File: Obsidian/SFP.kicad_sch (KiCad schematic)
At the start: 42 parts, among them J1 TYCO_1888247-1, J12 TYCO_1888247-1, J8 2180739-1, U17 TCA9555RTWR, U26 PCA9546ARGV

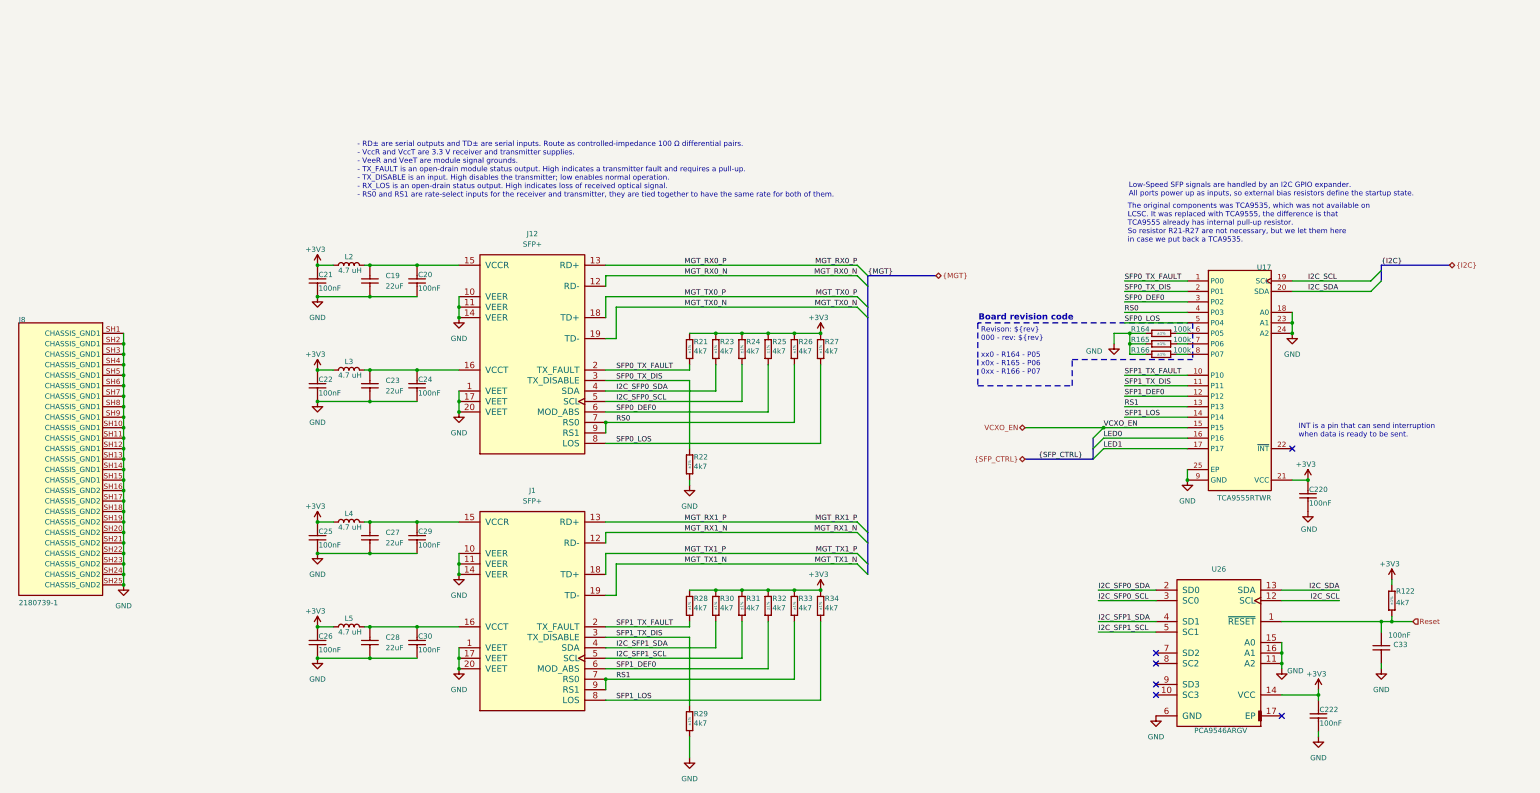
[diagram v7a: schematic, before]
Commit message: Cleaning symbol fields
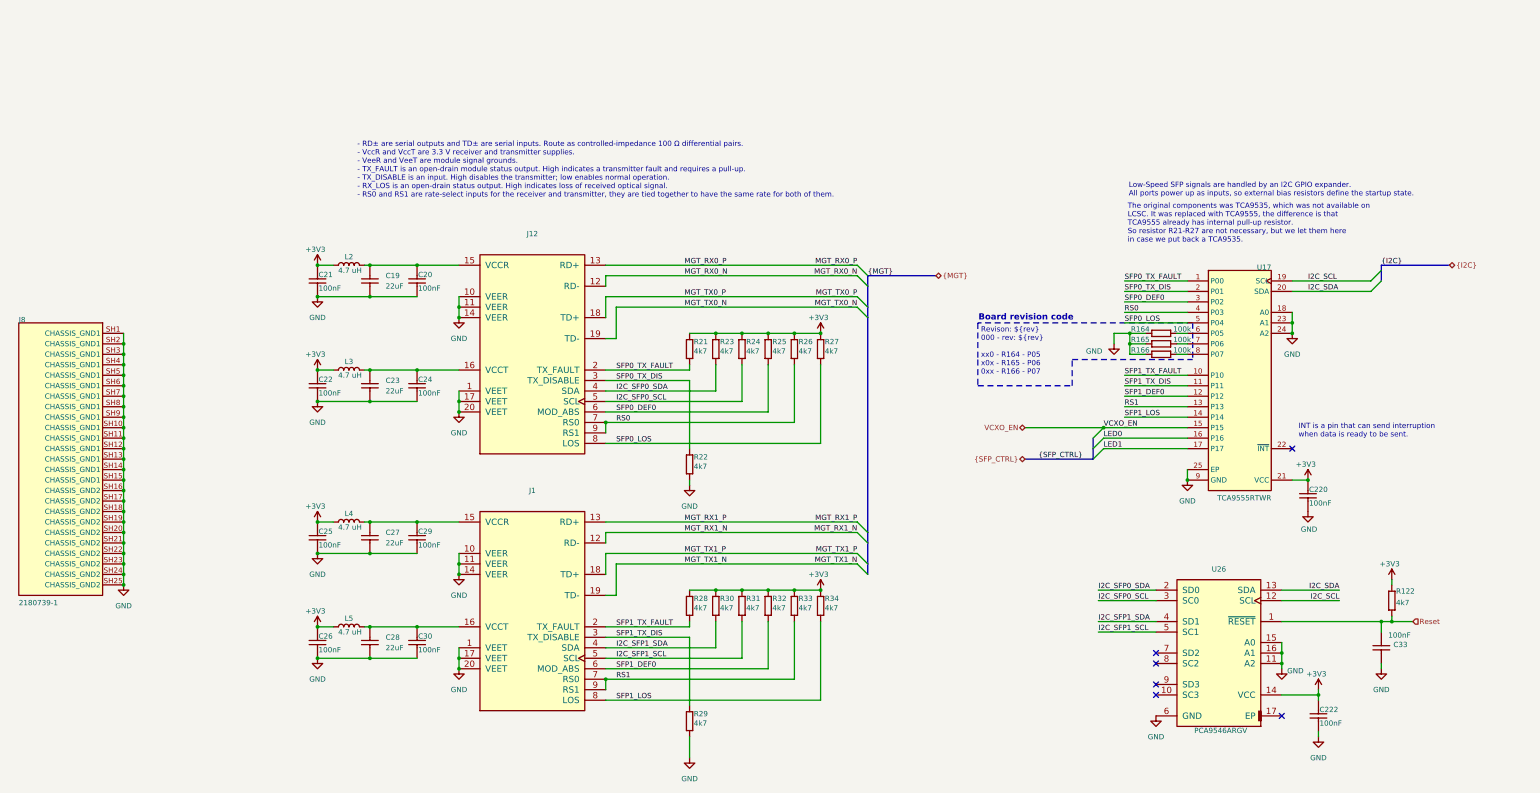
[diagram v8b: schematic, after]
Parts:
- C19, C23, C27, C28: Author CERN DEM JLC -> (none); Case 0805 -> (none); Comment 22uF -> (none); Component Kind Standard -> (none); Component Type Standard -> (none); ComponentHeight (none) -> (none); CreateDate 10/25/12 00:00:00 -> (none); Database Table Name Capacitors -> (none); Footprint Library Capacitors SMD -> (none); Footprint Path PcbLib\Capacitors SMD.PcbLib -> (none); Footprint Ref CAPC2012X135N -> (none); HelpURL \\cern.ch\dfs\Applications\Altium\Datasheets\CC0805_X5R_TDK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 -> (none); LatestRevisionDate 10/25/12 00:00:00 -> (none); Library Name Capacitors SMD -> (none); Library Path SchLib\Capacitors.SchLib -> (none); Library Ref Capacitor - non polarized -> (none); License CC-BY-SA 4.0 -> (none); Manufacturer GENERIC -> (none); Manufacturer Part Number CC0805_22UF_16V_10%_X5R -> (none); Manufacturer1 ComponentHeight 1.35mm -> (none); Manufacturer1 Example TDK -> (none); Manufacturer1 Part Number C2012X5R1C226KT -> (none); Mounted Yes -> (none); PackageDescription (none) -> (none); Part Description SMD Multilayer Chip Ceramic Capacitor -> (none); Part Number CC0805_22UF_16V_10%_X5R -> (none); Pin Count 2 -> (none); PressFit (none) -> (none); SMD Yes -> (none); Sense No -> (none); Sense Comment (none) -> (none); Socket No -> (none); Status Preferred -> (none); Status Comment (none) -> (none); TC X5R -> (none); Tolerance ±10% -> (none); Voltage 16V -> (none)
- C20, C21, C22, C220, C222, C24, C25, C26, C29, C30, C33: Author CERN DEM MR -> (none); Case 0402 -> (none); Comment 100nF -> (none); Component Kind Standard -> (none); Component Type Standard -> (none); ComponentHeight (none) -> (none); CreateDate 06/30/17 00:00:00 -> (none); Database Table Name Capacitors -> (none); Footprint Library Capacitors SMD -> (none); Footprint Path PcbLib\Capacitors SMD.PcbLib -> (none); Footprint Ref CAPC1005X55N -> (none); HelpURL \\cern.ch\dfs\Applications\Altium\Datasheets\CC0402_MURATA_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 -> (none); LatestRevisionDate 06/30/17 00:00:00 -> (none); Library Name Capacitors SMD -> (none); Library Path SchLib\Capacitors.SchLib -> (none); Library Ref Capacitor - non polarized -> (none); License CC-BY-SA 4.0 -> (none); Manufacturer GENERIC -> (none); Manufacturer Part Number CC0402_100NF_50V_10%_X7R -> (none); Manufacturer1 ComponentHeight 0.55mm -> (none); Manufacturer1 Example MURATA -> (none); Manufacturer1 Part Number GRM155R71H104KE14D -> (none); Mounted Yes -> (none); PackageDescription (none) -> (none); Part Description SMD Multilayer Chip Ceramic Capacitor -> (none); Part Number CC0402_100NF_50V_10%_X7R -> (none); Pin Count 2 -> (none); PressFit (none) -> (none); SMD Yes -> (none); Sense No -> (none); Sense Comment (none) -> (none); Socket No -> (none); Status None -> (none); Status Comment (none) -> (none); TC X7R -> (none); Tolerance ±10% -> (none); Voltage 50V -> (none)
- J1, J12: Author CERN DEM JLC -> (none); Case (none) -> (none); Comment (none) -> (none); Component Kind Standard -> (none); Component Type Standard -> (none); ComponentHeight 5.4mm -> (none); ComponentLink1Description (none) -> (none); ComponentLink1URL (none) -> (none); ComponentLink2Description (none) -> (none); ComponentLink2URL (none) -> (none); CreateDate 02/27/12 00:00:00 -> (none); Database Table Name Connectors -> (none); Device (none) -> (none); Family SFP+ -> (none); Footprint Library TYCO SMD -> (none); Footprint Path PcbLib\TYCO SMD.PcbLib -> (none); Footprint Ref TYCO_1888247-1 -> (none); HelpURL \\cern.ch\dfs\Applications\Altium\Datasheets\TYCO_1888247-1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 -> (none); LatestRevisionDate 02/27/12 00:00:00 -> (none); Library Name TYCO -> (none); Library Path SchLib\Connectors.SchLib -> (none); Library Ref SFP+x1 -> (none); License CC-BY-SA 4.0 -> (none); Manufacturer TYCO ELECTRONICS -> (none); Manufacturer Part Number 1888247-1 -> (none); Mounted Yes -> (none); PackageDescription (none) -> (none); Part Description 20 Position, Pitch 0.8mm SFP+ Receptacle (Small Form-factor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 -> (none); Part Number TYCO_1888247-1 -> (none); Pin Count 20 -> (none); PressFit No -> (none); SCEM (none) -> (none); SMD Yes -> (none); Sense No -> (none); Sense Comment (none) -> (none); Socket No -> (none); Status None -> (none); Status Comment (none) -> (none)
- J8: ALTIUM_VALUE * -> (none); CHECK_PRICES https://www.snapeda.com/parts/2180739-1/TE+Connectivity/vie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 -> (none); EU_ROHS_COMPLIANCE Compliant -> (none); MF TE Connectivity -> (none); MP 2180739-1 -> (none); PACKAGE None -> (none); SNAPEDA_LINK https://www.snapeda.com/parts/2180739-1/TE+Connectivity/vie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 -> (none)
- R122, R21, R22, R23, R24, R25, R26, R27, R28, R29, R30, R31, R32, R33, R34: Author CERN DEM JLC -> (none); Case 0402 -> (none); Comment 4k7 -> (none); Component Kind Standard -> (none); Component Type Standard -> (none); ComponentHeight (none) -> (none); CreateDate 12/03/07 00:00:00 -> (none); Database Table Name Resistors -> (none); Footprint Library Resistors SMD -> (none); Footprint Path PcbLib\Resistors SMD.PcbLib -> (none); Footprint Ref RESC1005X40N -> (none); HelpURL \\cern.ch\dfs\Applications\Altium\Datasheets\R0402_Phycomp_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 -> (none); LatestRevisionDate 10/17/12 00:00:00 -> (none); Library Name Resistors SMD -> (none); Library Path SchLib\Resistors.SchLib -> (none); Library Ref Resistor - 1% -> (none); License CC-BY-SA 4.0 -> (none); Manufacturer GENERIC -> (none); Manufacturer Part Number R0402_4K7_1%_0.0625W_100PPM -> (none); Manufacturer1 ComponentHeight 0.4mm -> (none); Manufacturer1 Example YAGEO PHYCOMP -> (none); Manufacturer1 Part Number 232270674702L -> (none); Mounted Yes -> (none); PackageDescription (none) -> (none); Part Description General Purpose Thick Film Chip Resistor -> (none); Part Number R0402_4K7_1%_0.0625W_100PPM -> (none); Pin Count 2 -> (none); Power 0.0625W -> (none); PressFit No -> (none); SMD Yes -> (none); Sense No -> (none); Sense Comment (none) -> (none); Socket No -> (none); Status Not Recommended -> (none); Status Comment (none) -> (none); TC ±100ppm/°C -> (none); Tolerance ±1% -> (none); Voltage (none) -> (none)
- R164, R165, R166: Author CERN DEM JLC -> (none); Case 0402 -> (none); Comment 100k -> (none); Component Kind Standard -> (none); Component Type Standard -> (none); ComponentHeight (none) -> (none); CreateDate 12/03/07 00:00:00 -> (none); Database Table Name Resistors -> (none); Footprint Library Resistors SMD -> (none); Footprint Path PcbLib\Resistors SMD.PcbLib -> (none); Footprint Ref RESC1005X40N -> (none); HelpURL \\cern.ch\dfs\Applications\Altium\Datasheets\R0402_Phycomp_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 -> (none); LatestRevisionDate 10/17/12 00:00:00 -> (none); Library Name Resistors SMD -> (none); Library Path SchLib\Resistors.SchLib -> (none); Library Ref Resistor - 1% -> (none); License CC-BY-SA 4.0 -> (none); Manufacturer GENERIC -> (none); Manufacturer Part Number R0402_100K_1%_0.0625W_100PPM -> (none); Manufacturer1 ComponentHeight 0.4mm -> (none); Manufacturer1 Example YAGEO PHYCOMP -> (none); Manufacturer1 Part Number 232270671004L -> (none); Mounted Yes -> (none); PackageDescription (none) -> (none); Part Description General Purpose Thick Film Chip Resistor -> (none); Part Number R0402_100K_1%_0.0625W_100PPM -> (none); Pin Count 2 -> (none); Power 0.0625W -> (none); PressFit No -> (none); SMD Yes -> (none); Sense No -> (none); Sense Comment (none) -> (none); Socket No -> (none); Status Not Recommended -> (none); Status Comment (none) -> (none); TC ±100ppm/°C -> (none); Tolerance ±1% -> (none); Voltage (none) -> (none)
- U17: # OF I/OS 16 -> (none); 5V TOLERANT I/O Yes -> (none); CODE_JEDEC MO-220 -> (none); COMPONENTLINK1DESCRIPTION Datasheet -> (none); COMPONENTLINK1URL http://www.ti.com/general/docs/lit/getliterature.tsp?generi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 -> (none); CONFIGURATION REGISTERS Yes -> (none); DATASHEETVERSION SCPS201A -> (none); ECO-PLAN Green (RoHS & no Sb/Br) -> (none); I2C ADDRESS 0100 xxx -> (none); INTERRUPT OUTPUT Yes -> (none); LOW POWER Yes -> (none); MANUFACTURER Texas Instruments -> (none); MAX FREQUENCY(KHZ) 400 -> (none); MOUNTING TECHNOLOGY Surface Mount -> (none); PACKAGEDESCRIPTION 24-Lead Plastic Quad FlatPack, No-Lead, 4x4x0.8mm Body [WQF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 -> (none); PACKAGEREFERENCE RTW0024B -> (none); PACKAGEVERSION Jul-04 -> (none); PARTNUMBER TCA9535RTWR -> (none); PUSH-PULL I/O TYPE Yes -> (none); SUBFAMILY I2C IO Expander -> (none); VCC RANGE(V) 1.65 to 5.5 -> (none)
- U26: Author CERN DEM HF -> (none); Bonding No -> (none); Case QFN16 -> (none); Comment PCA9546ARGV -> (none); Component Kind Standard -> (none); Component Type Standard -> (none); ComponentHeight 1mm -> (none); ComponentLink1Description (none) -> (none); ComponentLink1URL (none) -> (none); ComponentLink2Description (none) -> (none); ComponentLink2URL (none) -> (none); CreateDate 04/12/23 00:00:00 -> (none); Database Table Name ICs And Semiconductors -> (none); Device PCA9546ARGV -> (none); Footprint Library ICs And Semiconductors SMD -> (none); Footprint Path PcbLib\ICs And Semiconductors SMD.PcbLib -> (none); Footprint Ref QFN65P400X400X100-17N-S225 -> (none); HelpURL \\cern.ch\dfs\Applications\Altium\Datasheets\PCA9546A.pdf -> (none); LatestRevisionDate 04/12/23 00:00:00 -> (none); Library Name Analog & Interface -> (none); Library Path SchLib\Analog & Interface.SchLib -> (none); Library Ref PCA9546ARGV -> (none); License CC-BY-SA 4.0 -> (none); Manufacturer TEXAS INSTRUMENTS -> (none); Manufacturer Part Number PCA9546ARGV -> (none); Mounted Yes -> (none); PackageDescription QFN, 0.65mm Pitch, Square; 16 Pin, 4.00mm L X 4.00mm W X 1.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 -> (none); Part Description Low Voltage 4-Channel I2C and SMBus Switch with Reset Funct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 -> (none); Part Number PCA9546ARGV -> (none); Pin Count 17 -> (none); PressFit No -> (none); SCEM (none) -> (none); SMD Yes -> (none); Sense No -> (none); Sense Comment (none) -> (none); Socket No -> (none); Status (none) -> (none); Status Comment (none) -> (none)
